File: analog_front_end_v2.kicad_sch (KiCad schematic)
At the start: 142 parts, among them J1 Conn_Coaxial, J3 Conn_01x01_Socket, J4 Conn_01x01_Socket, T1 JTX-4-10T_, U1 ADL5531, U10 PMOD 2x6, U11 LP2985-5.0, U12 LP2985-5.0, U14 MAX 735, U15 LP2985-2.5, U16 MAX889SESA, U17 MAX6102, U18 PAT1220-C-0DB, U19 PAT1220-C-0DB, U2 ADL5531, U20 PAT1220-C-0DB, U21 PAT1220-C-0DB, U22 LP2985-3.3, U23 PMOD 2x6, U24 ADA4899-1YRDZ, U25 ADA4899-1YRDZ, U26 ADA4899-1YRDZ, U3 ADL5531, U4 ADA4899-1YRDZ, U5 ADF4360-9, U6 LTC1406, U9 PMOD 2x6

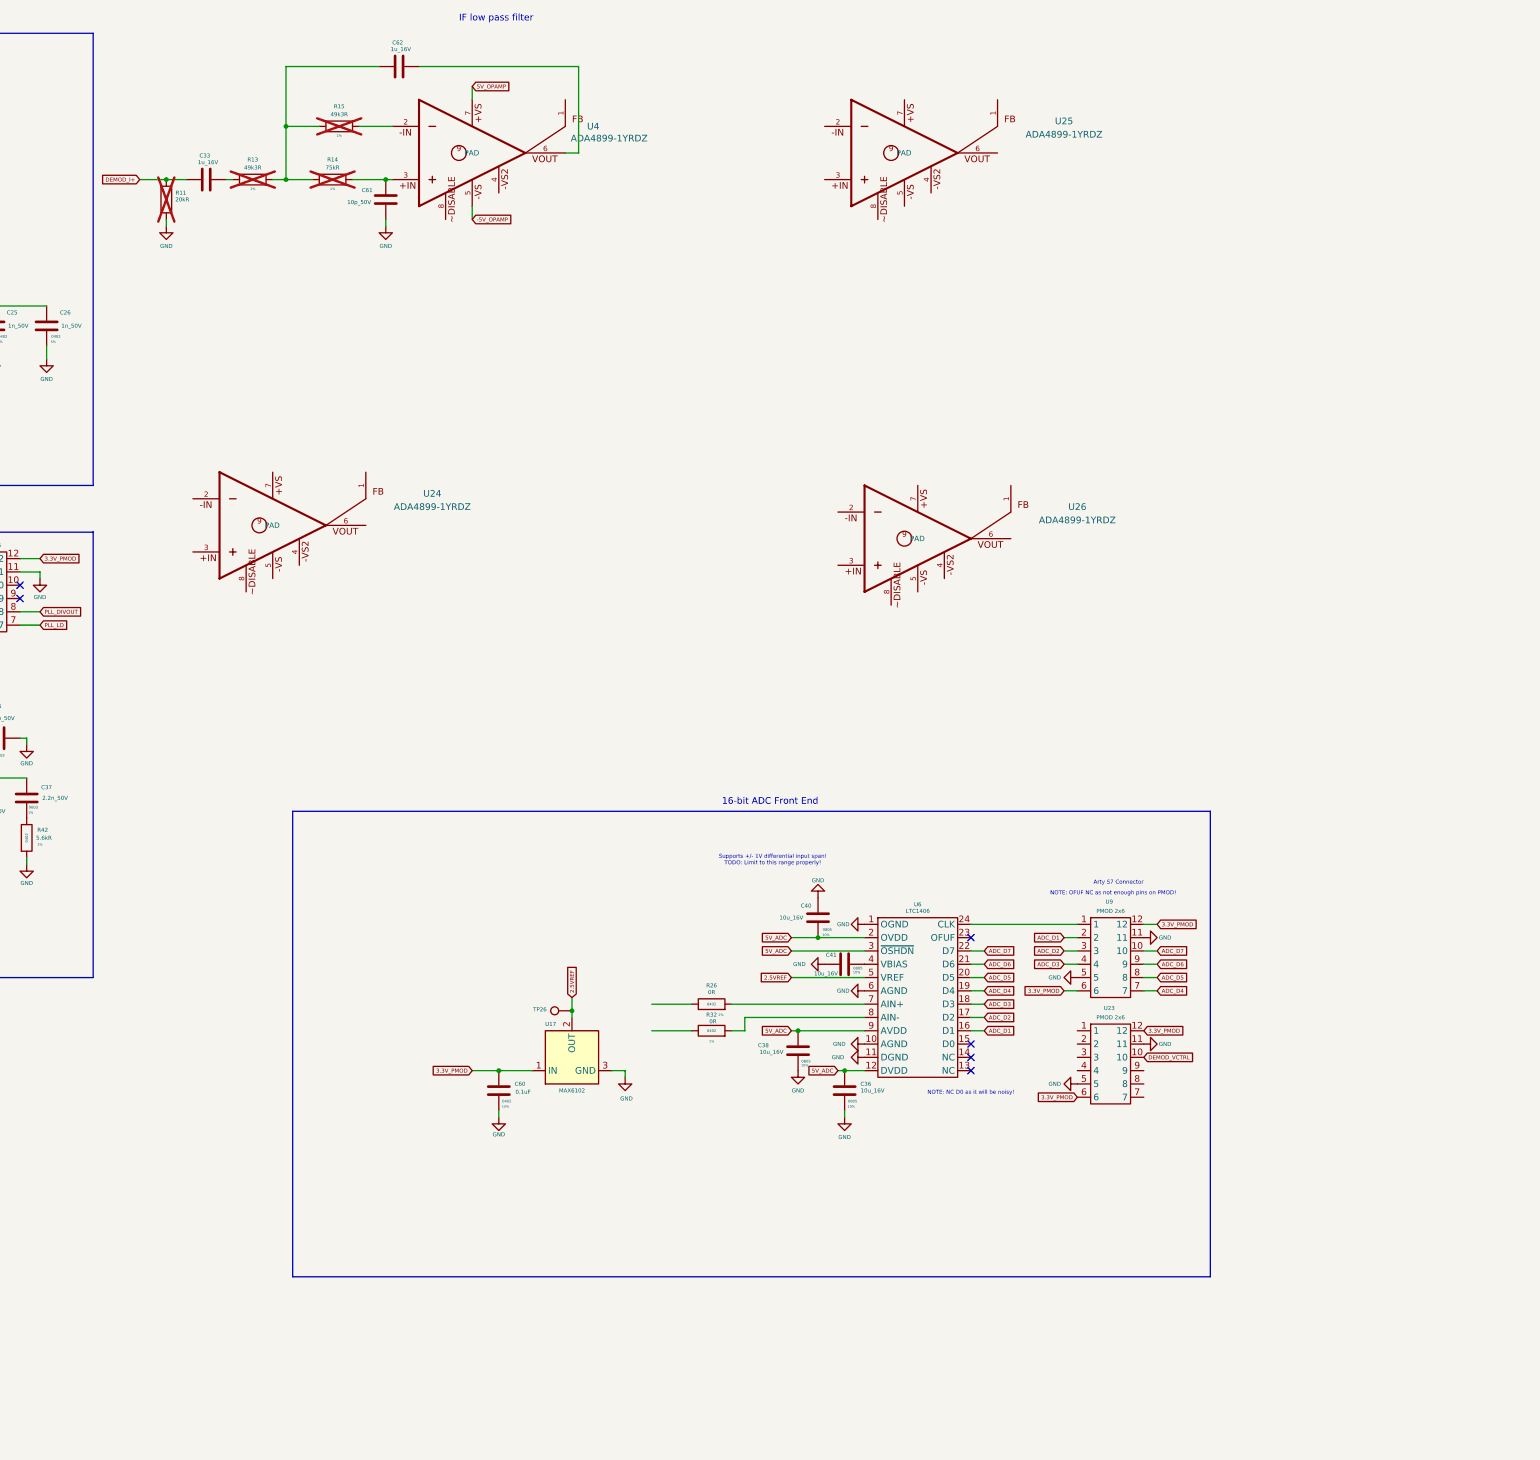
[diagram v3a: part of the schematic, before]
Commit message: Finish off IF filter section
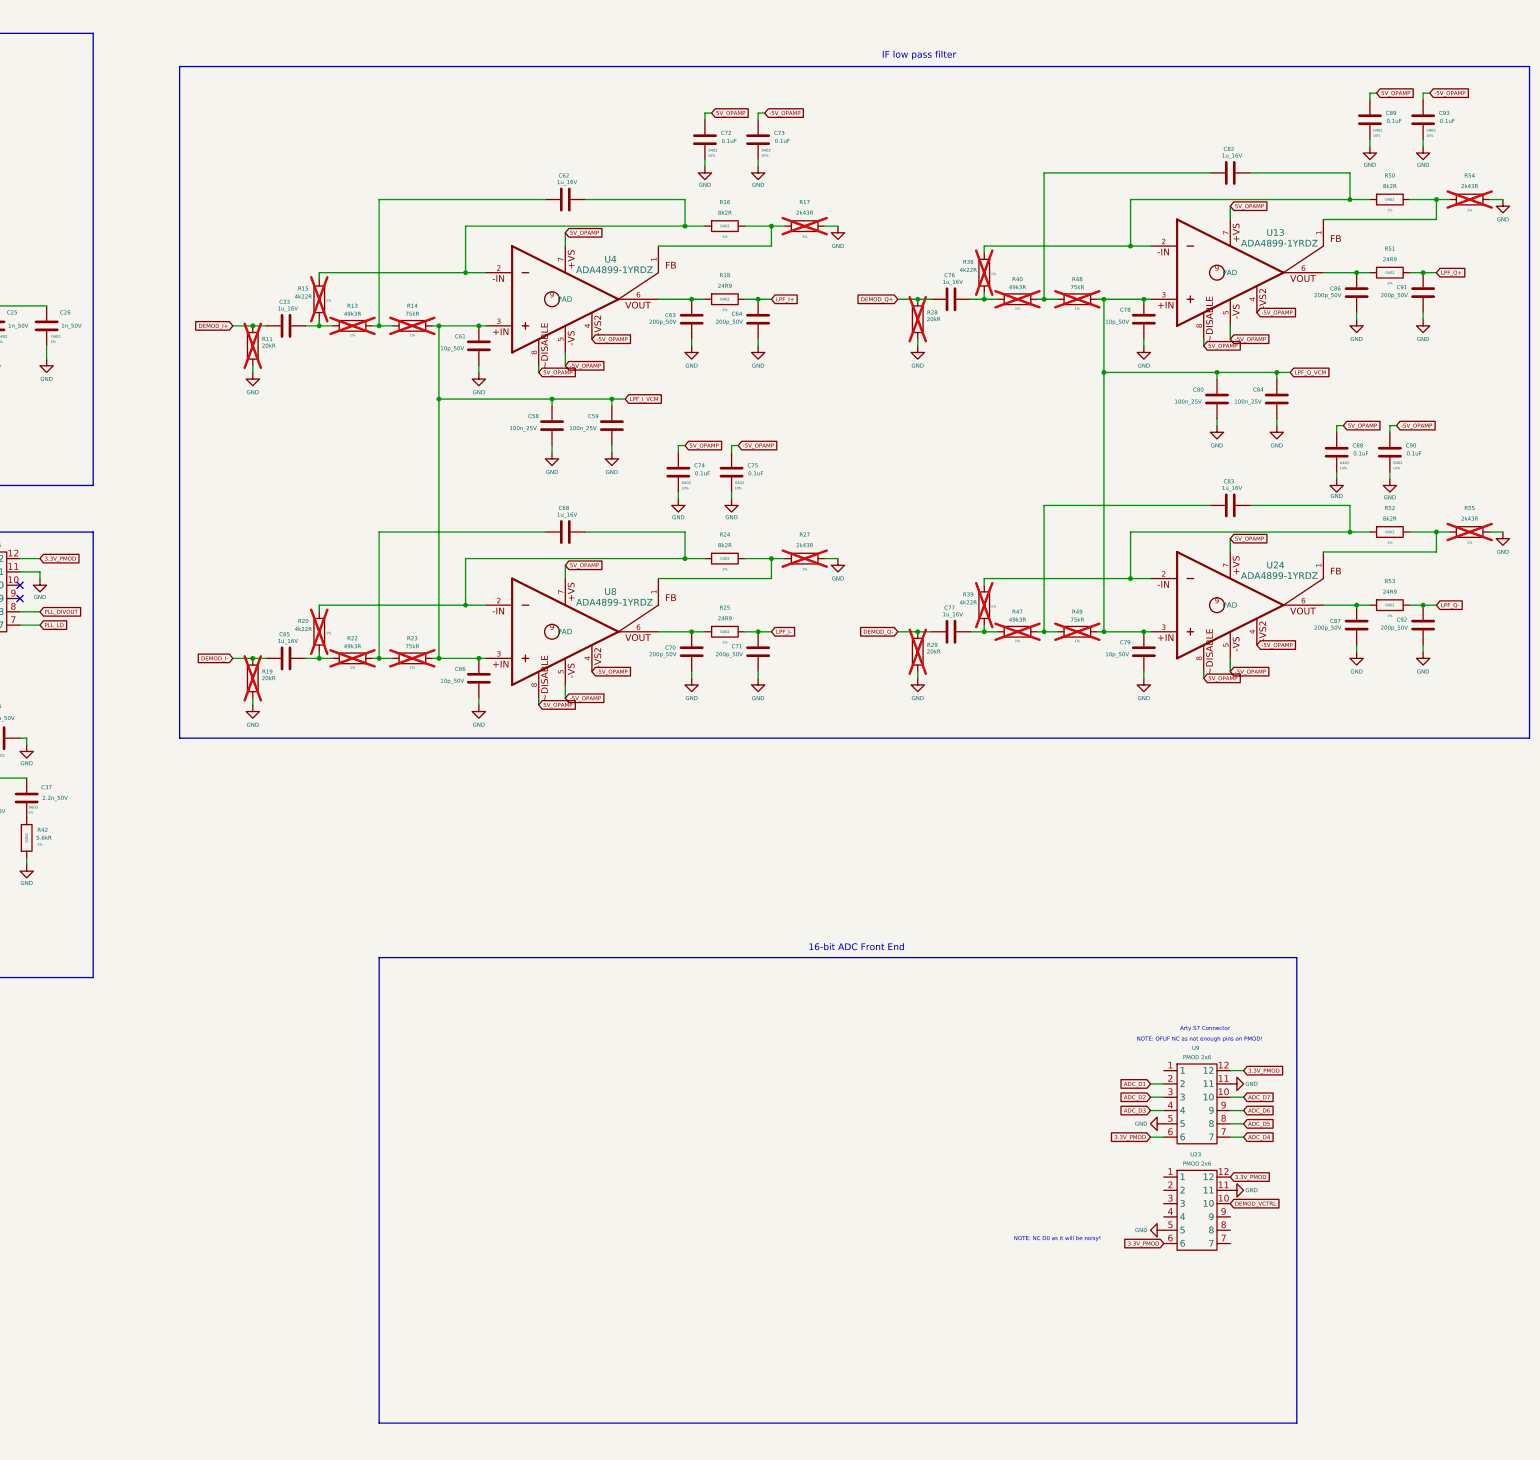
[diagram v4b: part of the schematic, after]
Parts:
- removed C36, C38, C40, C41: 10u_16V, Capacitor_SMD:C_0805_2012Metric, symbol Device:C
- removed C60: 0.1uF, Capacitor_SMD:C_0402_1005Metric, symbol Device:C
- removed R26, R32: 0R, Resistor_SMD:R_0402_1005Metric, symbol Device:R
- removed TP26: TestPoint, TestPoint:TestPoint_Pad_D1.0mm, symbol Connector:TestPoint
- removed U17: MAX6102, Package_TO_SOT_SMD:SOT-23, symbol Reference_Voltage:MAX6102
- removed U25, U26: ADA4899-1YRDZ, ADA4899-1YRDZ:SOIC127P600X175-9N, symbol ADA4899-1YRDZ:ADA4899-1YRDZ
- removed U6: LTC1406, TheEEView_Footprint_Lib:LTC1406, symbol TheEEView_Global_Lib:LTC1406
- added C58, C59, C80, C84: 100n_25V, Capacitor_SMD:C_0402_1005Metric, symbol Device:C
- added C63, C64, C70, C71, C86, C87, C91, C92: 200p_50V, Capacitor_SMD:C_0402_1005Metric, symbol Device:C
- added C65, C68, C76, C77, C82, C83: 1u_16V, Capacitor_SMD:C_0402_1005Metric, symbol Device:C
- added C66, C78, C79: 10p_50V, Capacitor_SMD:C_0402_1005Metric, symbol Device:C
- added C72, C73, C74, C75, C88, C89, C90, C93: 0.1uF, Capacitor_SMD:C_0402_1005Metric, symbol Device:C
- added R16, R24, R50, R52: 8k2R, Resistor_SMD:R_0402_1005Metric, symbol Device:R
- added R17, R27, R54, R55: 2k43R, Resistor_SMD:R_0402_1005Metric, symbol Device:R
- added R18, R25, R51, R53: 24R9, Resistor_SMD:R_0402_1005Metric, symbol Device:R
- added R19, R28, R29: 20kR, Resistor_SMD:R_0402_1005Metric, symbol Device:R
- added R20, R38, R39: 4k22R, Resistor_SMD:R_0402_1005Metric, symbol Device:R
- added R22, R40, R47: 49k3R, Resistor_SMD:R_0402_1005Metric, symbol Device:R
- added R23, R48, R49: 75kR, Resistor_SMD:R_0402_1005Metric, symbol Device:R
- added U13, U8: ADA4899-1YRDZ, ADA4899-1YRDZ:SOIC127P600X175-9N, symbol ADA4899-1YRDZ:ADA4899-1YRDZ
- C61: MOC GRM1555C1H102JA01D -> (none)
- R11: MOC RC0402FR-0720KL -> (none)
- R15: value 49k3R -> 4k22R
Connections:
- net -5V_OPAMP: now also U24.4, U24.5, U4.4, C73.2, C75.2, C90.2, C93.2, U13.4, U13.5, U8.4, U8.5
- net 5V_OPAMP: now also U24.7, U24.8, U4.8, C72.2, C74.2, C88.2, C89.2, U13.7, U13.8, U8.7, U8.8
- net DEMOD_I-: now also C65.1, R19.1
- net DEMOD_Q+: now also C76.1, R28.1
- net DEMOD_Q-: now also C77.1, R29.1
- net GND: now also C58.2, C59.2, C63.2, C64.2, C66.2, C70.2, C71.2, C72.1, C73.1, C74.1, C75.1, C78.2, C79.2, C80.2, C84.2, C86.2, C87.2, C88.1, C89.1, C90.1, C91.2, C92.2, C93.1, R17.1, R19.2, R27.1, R28.2, R29.2, R54.1, R55.1
- net at C33.2, R13.1: now also R15.1
- net at C62.1, R13.2, R14.1: no longer R15.1
- net at U24.1: now also R52.1, R55.2
- net at U24.2: now also C83.2, R39.2, R52.2
- net LPF_Q_VCM: now reaches U24.3
- net LPF_Q_VCM: now also C78.1, C79.1, C80.1, C84.1, R48.2, R49.2, U13.3
- net at U24.6: now also C87.1, R53.2
- net LPF_I_VCM: now reaches C61.1, R14.2, U4.3
- net LPF_I_VCM: now also C58.1, C59.1, C66.1, R23.2, U8.3
- net at R15.2, U4.2: now also C62.2, R16.2
- net at U4.1: now also R16.1, R17.2
- net at U4.6: now also C63.1, R18.2; no longer C62.2
- new net: R50.1, R54.2, U13.1
- new net: C82.2, R38.2, R50.2, U13.2
- new net: C77.2, R39.1, R47.1
- new net: C83.1, R47.2, R49.1
- new net: R24.1, R27.2, U8.1
- new net: C68.2, R20.2, R24.2, U8.2
- new net: C70.1, R25.2, U8.6
- new net: C76.2, R38.1, R40.1
- new net: C82.1, R40.2, R48.1
- new net: C65.2, R20.1, R22.1
- new net: C86.1, R51.2, U13.6
- new net: C68.1, R22.2, R23.1
- new net LPF_I+: C64.1, R18.1
- new net LPF_I-: C71.1, R25.1
- new net LPF_Q+: C91.1, R51.1
- new net LPF_Q-: C92.1, R53.1
- no-connect marks 23 -> 19
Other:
- note removed: "Supports +/- 1V differential input span! TODO: Limit to this range properly!"
- moved on the sheet: C33, C61, C62, R11, R13, R14, R15, U23, U4, U9

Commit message: Begin drawing I/Q ADC section
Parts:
- removed C55, C56: 4.7u_16V, Capacitor_SMD:C_1206_3216Metric, symbol Device:C_Polarized_US
- removed U16: MAX889SESA, Package_SO:SOIC-8_5.3x5.3mm_P1.27mm, symbol TheEEView_Global_Lib:MAX889
- added C36, C38, C56, C67, C69: 10u_16V, Capacitor_SMD:C_0805_2012Metric, symbol Device:C
- added C40, C41, C55, C60, C81, C85: 0.1uF, Capacitor_SMD:C_0402_1005Metric, symbol Device:C
- added R26, R32: 50R, Resistor_SMD:R_0402_1005Metric, symbol Device:R
- added U16, U6: ~, symbol TheEEView_Global_Lib:LTC2386
- C57: value 1u_16V -> 10u_16V; footprint Capacitor_SMD:C_0603_1608Metric -> Capacitor_SMD:C_0805_2012Metric; MOC 0603YC105JAT2A -> CL21B106KOQNNNE; Size 0603 -> 0805; Tolerance 5% -> 10%
- R36: value 100k -> 50R; MOC ERJ-2RKF1003X -> CRCW060350R0FKEA
- R37: value 66.5k -> 50R; MOC CRCW040266K5FKEDC -> CRCW060350R0FKEA
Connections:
- net 5V_ADC: now also C36.2, C40.2, C67.2, C81.2, U16.11 (VDD), U16.12 (VDD), U6.11 (VDD), U6.12 (VDD)
- net 5V_LNA: no longer R36.2
- net GND: now also C57.1, C36.1, C38.1, C40.1, C41.1, C55.1, C56.1, C60.1, C67.1, C69.1, C81.1, C85.1, U16.1 (GND), U16.10 (GND), U16.21 (GND), U16.26 (GND), U16.29 (GND), U16.4 (GND), U16.7 (REFBUF), U16.8 (REFBUF), U6.1 (GND), U6.10 (GND), U6.21 (GND), U6.26 (GND), U6.29 (GND), U6.4 (GND), U6.7 (REFBUF), U6.8 (REFBUF)
- net LPF_I+: now also U6.2 (IN+)
- net LPF_I-: now also U6.3 (IN-)
- net LPF_I_VCM: now also U6.32 (VCM)
- net LPF_Q+: now also U16.2 (IN+)
- net LPF_Q-: now also U16.3 (IN-)
- net LPF_Q_VCM: now also U16.32 (VCM)
- net ADC_Q_CNV+: now reaches R36.1
- net ADC_Q_CNV+: now also U16.28 (CNV+); no longer R37.2
- net at C57.2: now also U16.5 (REFGND), U16.6 (REFGND)
- net -2.5V_DiffAmp: no longer names the net of R37.1
- net -2.5V_DiffAmp: now also R36.2
- net 2.5V_DiffAmp renamed 2V5_ADC
- net 2V5_ADC: now also C38.2, C41.2, C69.2, C85.2, U16.30 (VDDL), U16.31 (VDDL), U6.30 (VDDL), U6.31 (VDDL)
- new net: R26.2, R32.1
- new net: C60.2, U16.9 (REFIN)
- new net: C56.2, U6.5 (REFGND), U6.6 (REFGND)
- new net: C55.2, U6.9 (REFIN)
- new net ADC_I_CNV+: R26.1, U6.28 (CNV+)
- new net ADC_I_CNV-: R32.2, U6.27 (CNV-)
- new net ADC_Q_CNV-: R37.2, U16.27 (CNV-)
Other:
- note added: "2x 16-bit ADC Front End for I/Q"
- note removed: "16-bit ADC Front End"
- moved on the sheet: U23, U9

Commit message: Completed schematic
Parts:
- removed R3: 50R, Resistor_SMD:R_0402_1005Metric, symbol Device:R
- removed TP23: TestPoint, TestPoint:TestPoint_Pad_D1.0mm, symbol Connector:TestPoint
- added R56, R57, R58, R59, R60, R61: 100R, Resistor_SMD:R_0402_1005Metric, symbol Device:R
- R26, R32, R36, R37, R4: value 50R -> 100R; MOC CRCW060350R0FKEA -> (none)
- U16, U6, U7: value ~ -> LT5546
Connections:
- net 2V5_ADC: now also U16.22 (OVDD), U6.22 (OVDD)
- net ADC_I_CNV-: now also R26.2; no longer R32.2
- net ADC_Q_CNV-: now also R36.2; no longer R37.2
- net DEMOD_VCTRL: now also R4.1
- net ADC_I_CLK+: now reaches R32.1
- net ADC_I_CLK+: now also U6.24 (CLK+); no longer R26.2
- net ADC_I_PDN: now reaches U6.13 (~{PD})
- net ADC_I_TESTPAT: now reaches U6.14 (TESTPAT)
- net ADC_I_DA-: now reaches U6.15 (DB-)
- net ADC_I_DA-: now also U6.17 (DA-), R56.2, R57.2
- net ADC_I_DA+: now reaches U6.16 (DB+)
- net ADC_I_DA+: now also U6.18 (DA+), R56.1, R57.1
- net ADC_I_DCO-: now reaches U6.19 (DCO-)
- net ADC_I_DCO-: now also R37.2
- net ADC_I_DCO+: now reaches U6.20 (DCO+)
- net ADC_I_DCO+: now also R37.1
- net ADC_I_CLK-: now reaches U6.23 (CLK-)
- net ADC_I_CLK-: now also R32.2
- net ADC_I_TWOLANES: now reaches U6.25 (TWOLANES)
- net ADC_Q_PDN: now reaches U16.13 (~{PD})
- net ADC_Q_TESTPAT: now reaches U16.14 (TESTPAT)
- net ADC_Q_DA-: now reaches U16.15 (DB-)
- net ADC_Q_DA-: now also U16.17 (DA-), R60.2, R61.2
- net ADC_Q_DA+: now reaches U16.16 (DB+)
- net ADC_Q_DA+: now also U16.18 (DA+), R60.1, R61.1
- net ADC_Q_DCO-: now reaches U16.19 (DCO-)
- net ADC_Q_DCO-: now also R59.2
- net ADC_Q_DCO+: now reaches U16.20 (DCO+)
- net ADC_Q_DCO+: now also R59.1
- net ADC_Q_CLK-: now reaches U16.23 (CLK-)
- net ADC_Q_CLK-: now also R58.2
- net ADC_Q_CLK+: now reaches U16.24 (CLK+)
- net ADC_Q_CLK+: now also R58.1
- net ADC_Q_TWOLANES: now reaches U16.25 (TWOLANES)
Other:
- note added: "88 - 108 MHz : 2nd order LC passive RF Band Pass Filter"
- note removed: "2nd order LC passive RF Band Pass Filter"
- moved on the sheet: C36, C38, C40, C41, C55, C56, C57, C60, C67, C69, C81, C85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

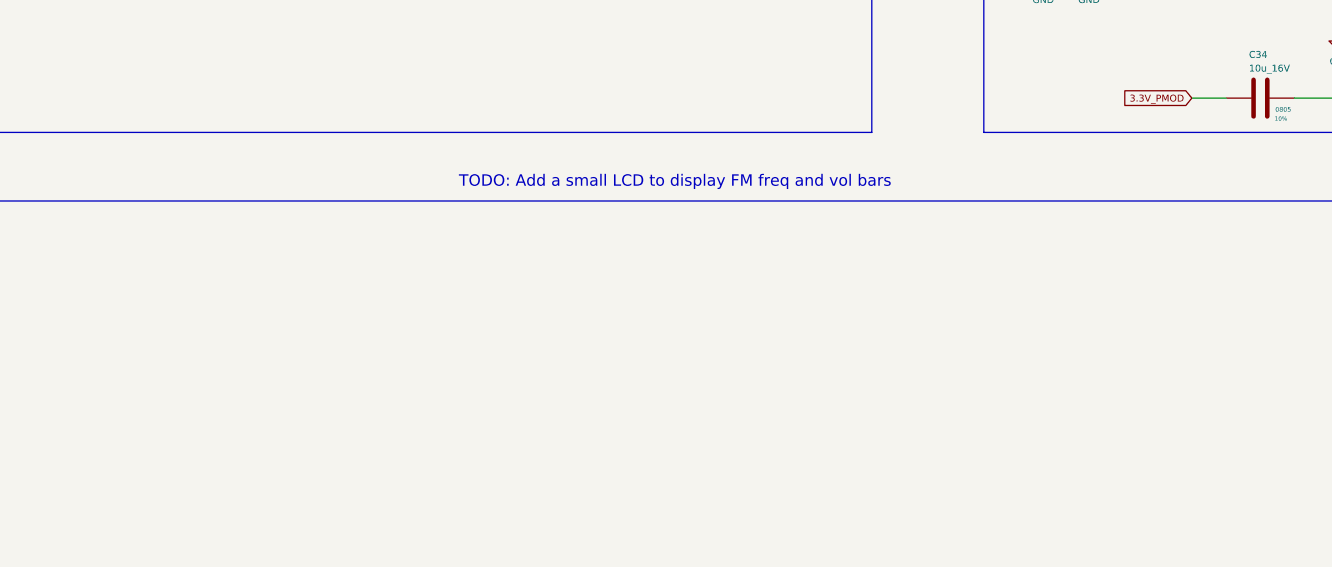
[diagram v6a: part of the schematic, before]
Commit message: Further optimisations of the RF frontend
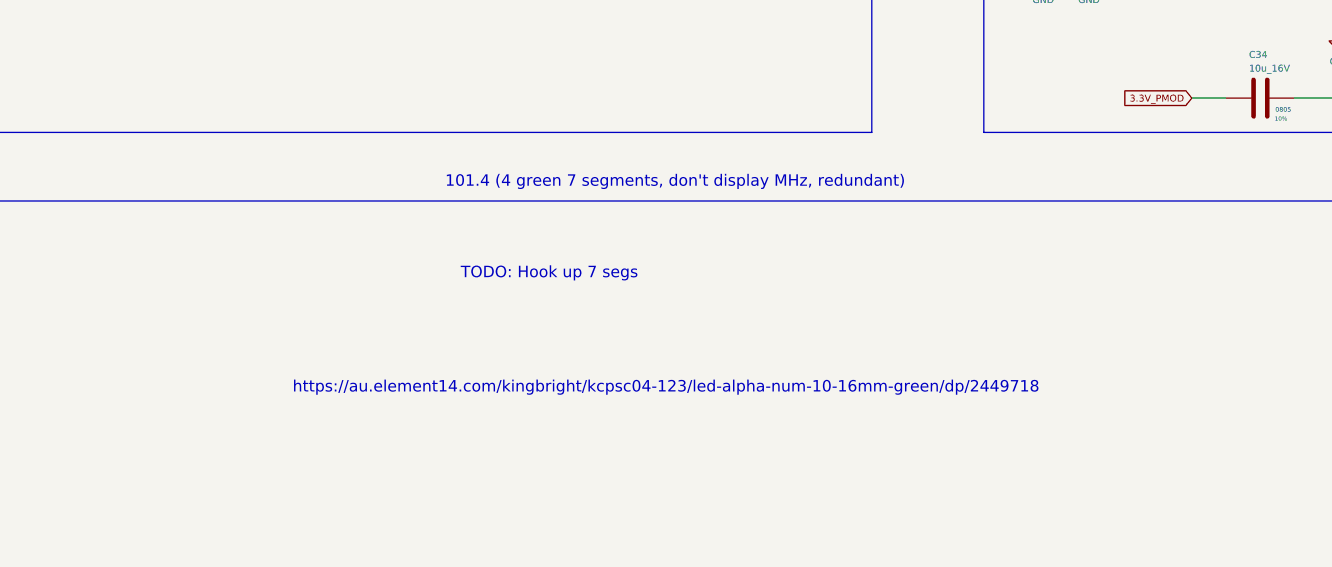
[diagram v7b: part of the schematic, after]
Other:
- note added: "101.4 (4 green 7 segments, don't display MHz, redundant)"
- note added: "TODO: Hook up 7 segs"
- note added: "https://au.element14.com/kingbright/kcpsc04-123/led-alpha-num-10-16mm-green/dp/2449718"
- note removed: "TODO: Add a small LCD to display FM freq and vol bars"
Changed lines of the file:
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@@
 		)
 	)
-	(text "TODO: Add a small LCD to display FM freq and vol bars"
+	(text "101.4 (4 green 7 segments, don't display MHz, redundant)"
 		(exclude_from_sim no)
 		(at 281.686 203.708 0)
@@
 		)
 	)
+	(text "https://au.element14.com/kingbright/kcpsc04-123/led-alpha-num-10-16mm-green/dp/2449718"
+		(exclude_from_sim no)
+		(at 280.67 226.568 0)
+		(effects
+			(font
+				(size 1.27 1.27)
+			)
+		)
+	)
 	(text "SMA Connector for FM antenna input"
 		(exclude_from_sim no)
@@
 			)
 		)
+	)
+	(text "TODO: Hook up 7 segs"
+		(exclude_from_sim no)
+		(at 267.716 213.868 0)
+		(effects
+			(font
+				(size 1.27 1.27)
+			)
+		)
